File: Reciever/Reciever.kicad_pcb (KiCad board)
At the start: 2 copper layers, 20 x 20 mm, 8 parts, among them J1 Conn_01x01_Socket, J2 Conn_01x02_Socket, J3 Conn_01x02_Socket, U2 LM393BIPWR, U3 LM386MX-1_NOPB

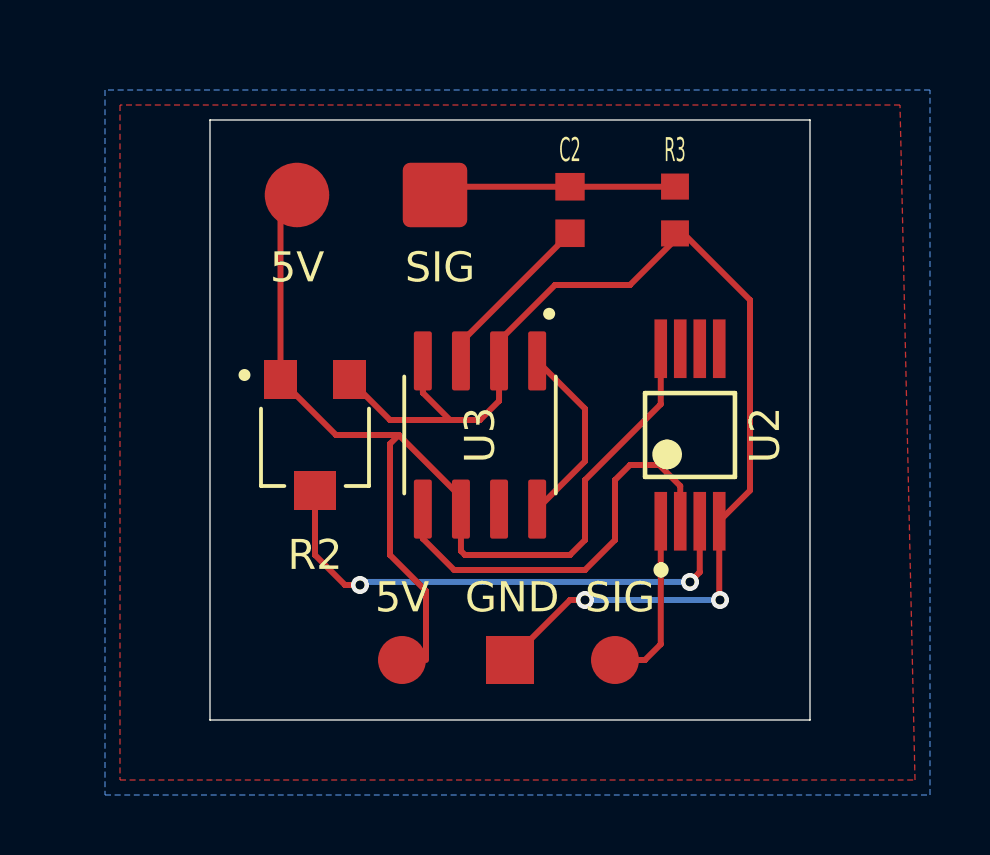
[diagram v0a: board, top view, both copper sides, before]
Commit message: updated to utilise more common parts
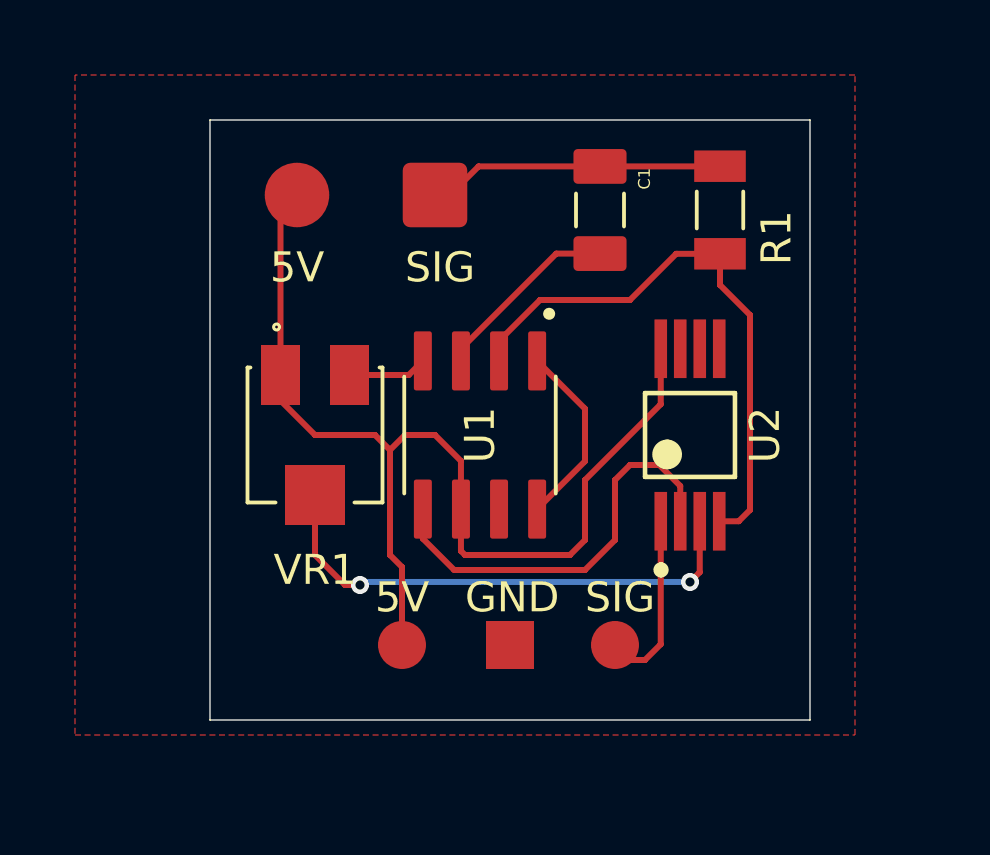
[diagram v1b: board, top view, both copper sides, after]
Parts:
- removed C2: 0603YC104KAZ2A, 0603YC104KAZ2A:CAPC1608X90N
- removed R2: PVG3G103C01R00, PVG3G103C01R00:TRIM_PVG3G103C01R00
- removed R3: CR0603AFX-1002EAS, CR0603AFX-1002EAS:RESC1608X55N
- added C1: CL31B104KBCNNNC, CL31B104KBCNNNC:CAPC3216X100N, F.Cu at (148.0, 38.5)
- added R1: 1206W4F1002T5E, 1206W4F1002T5E:RESC3115X65N, F.Cu at (152.0, 38.5)
- added VR1: 3314J-1-100E, 3314J-1-100E:TRIM_3314J-1-100E, F.Cu at (138.5, 46.0)
- moved J1 0.50 mm to (148.5, 53.0)
- moved J3 0.50 mm to (141.4, 53.0)
- renumbered U3 to U1
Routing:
- net GND: track 39.3 -> 22.0 mm, vias 2 -> 0
- net Net-(J2-Pin_1): track 8.12 -> 9.90 mm
- net Net-(U1-+INPUT): track 5.76 -> 6.97 mm
- removed copper zone on B.Cu, net GND

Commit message: updated pcb, removed dead traces
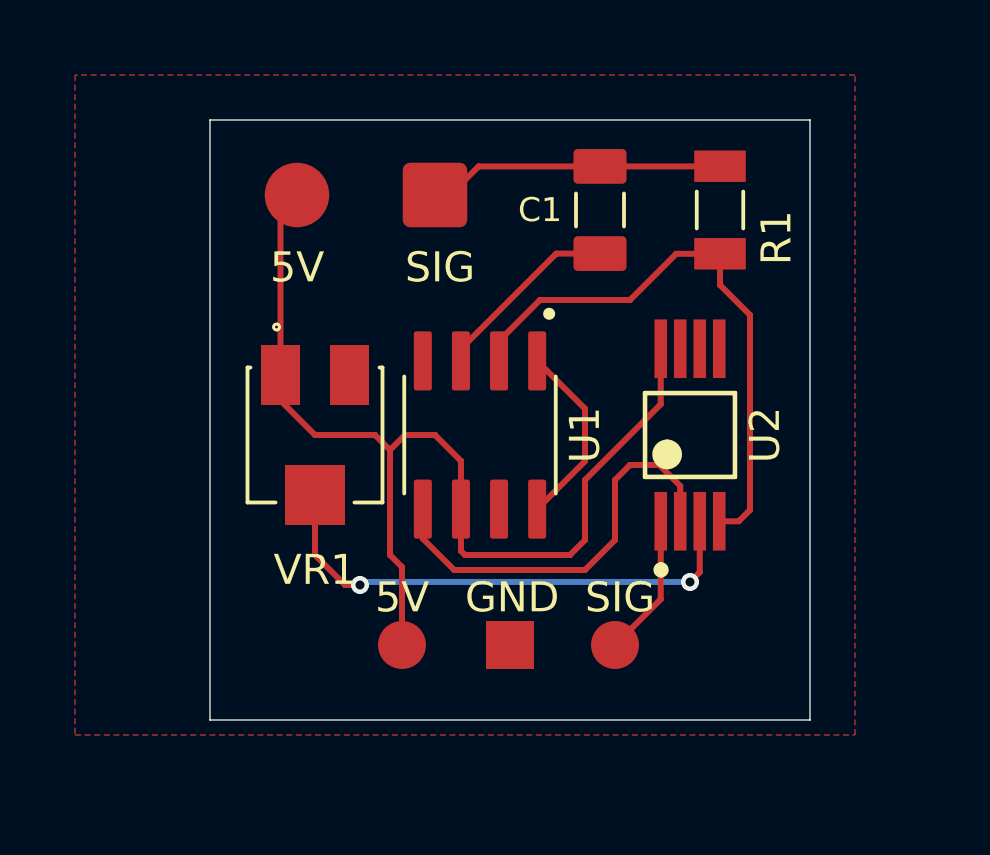
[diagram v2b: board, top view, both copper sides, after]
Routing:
- net GND: track 22.0 -> 19.4 mm
- net Net-(J1-Pin_1): track 5.84 -> 4.76 mm
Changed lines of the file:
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@@
 		(at 148 38.5 -90)
 		(property "Reference" "C1"
-			(at -1.04 -1.48 90)
+			(at 0 2 180)
 			(layer "F.SilkS")
 			(effects
 				(font
-					(size 0.393701 0.393701)
-					(thickness 0.15)
+					(size 0.8 0.8)
+					(thickness 0.098425)
 				)
 			)
@@
 			(at 0.96 1.48 90)
 			(layer "F.Fab")
+			(hide yes)
 			(effects
 				(font
@@
 		(at 144 46 -90)
 		(property "Reference" "U1"
-			(at 0 0 90)
+			(at 0 -3.5 90)
 			(layer "F.SilkS")
 			(effects
@@
 	(segment
 		(start 150.025 48.87538)
-		(end 150.025 52.975)
+		(end 150.025 51.475)
 		(width 0.2)
 		(layer "F.Cu")
@@
 	)
 	(segment
-		(start 150.025 52.975)
-		(end 149.5 53.5)
-		(width 0.2)
-		(layer "F.Cu")
-		(net 5)
-	)
-	(segment
-		(start 149.5 53.5)
-		(end 148.5 53.5)
+		(start 150.025 51.475)
+		(end 148.5 53)
 		(width 0.2)
 		(layer "F.Cu")
@@
 	)
 	(segment
-		(start 141.625 44)
-		(end 142.095 43.53)
-		(width 0.2)
-		(layer "F.Cu")
-		(net 7)
-	)
-	(segment
 		(start 150.54 39.96)
 		(end 149 41.5)
@@
 		(width 0.2)
 		(layer "F.Cu")
-		(net 7)
-	)
-	(segment
-		(start 139.65 44)
-		(end 141.625 44)
-		(width 0.2)
-		(layer "F.Cu")

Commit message: Updated to add resistor pad for gain, and 5v flood to CL2
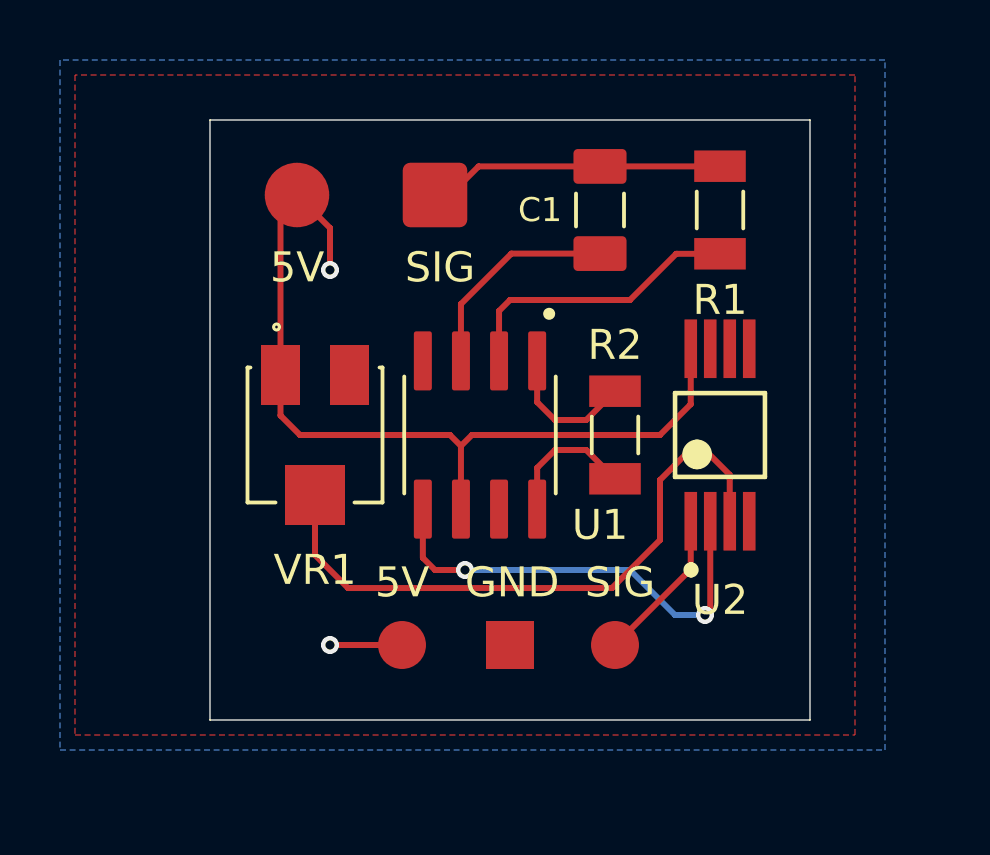
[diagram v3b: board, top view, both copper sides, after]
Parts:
- added R2: 1206W4F1002T5E, 1206W4F1002T5E:RESC3115X65N, F.Cu at (148.5, 46.0)
- J2: value Conn_01x02_Socket -> Piezo pins
- J3: value Conn_01x02_Socket -> Board Power
- moved U2 1.00 mm to (152.0, 46.0)
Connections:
- U1 pad 1: Net-(U1-GAIN-Pad1) -> Net-(R2-Pad1)
- U1 pad 8: Net-(U1-GAIN-Pad1) -> Net-(R2-Pad2)
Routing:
- net GND: track 19.4 -> 9.82 mm
- net Net-(U1-GAIN-Pad1): track 6.26 -> 0.00 mm
- net Net-(R2-Pad2): track 0.00 -> 4.61 mm
- net Net-(R2-Pad1): track 0.00 -> 4.61 mm
- net +5V: track 35.8 -> 31.6 mm, vias 0 -> 2
- net Net-(U2-Pad3): track 17.1 -> 21.3 mm, vias 2 -> 0
- net Net-(U1-VOUT): track 14.1 -> 15.0 mm, vias 0 -> 2
- added copper zone on B.Cu, net +5V
